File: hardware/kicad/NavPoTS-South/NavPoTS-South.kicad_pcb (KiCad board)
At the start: 4 copper layers, 58.9 x 58.9 mm, 119 parts, among them J1 Screw_Terminal_01x02, J10 Conn_01x03_Pin, J11 Conn_01x03_Pin, J12 Conn_01x03_Pin, J13 Conn_01x03_Pin, J14 Conn_01x03_Pin, J15 Conn_01x03_Pin, J16 Conn_01x03_Pin, J17 Screw_Terminal_01x02, J18 Conn_02x04_Top_Bottom, J19 Conn_02x04_Top_Bottom, J2 Screw_Terminal_01x02, J20 Screw_Terminal_01x02, J21 Screw_Terminal_01x02, J22 Conn_02x04_Top_Bottom, J23 62684-402100ALF, J24 Conn_02x04_Top_Bottom, J25 Screw_Terminal_01x02, J26 Screw_Terminal_01x02, J4 Screw_Terminal_01x02, J5 Screw_Terminal_01x02, J9 Conn_01x03_Pin, Q1 Q_NMOS_GSD, Q10 AO4576, Q11 AO4576, Q12 AO4576, Q13 AO4576, Q3 Q_NMOS_GSD, Q5 SI4143DY-T1-GE3, Q7 SI4143DY-T1-GE3, Q9 SI4143DY-T1-GE3, U1 SIC431A, U2 AP64501SP-13, U3 LTC4412xS6, U4 AP64501SP-13, U5 INA226

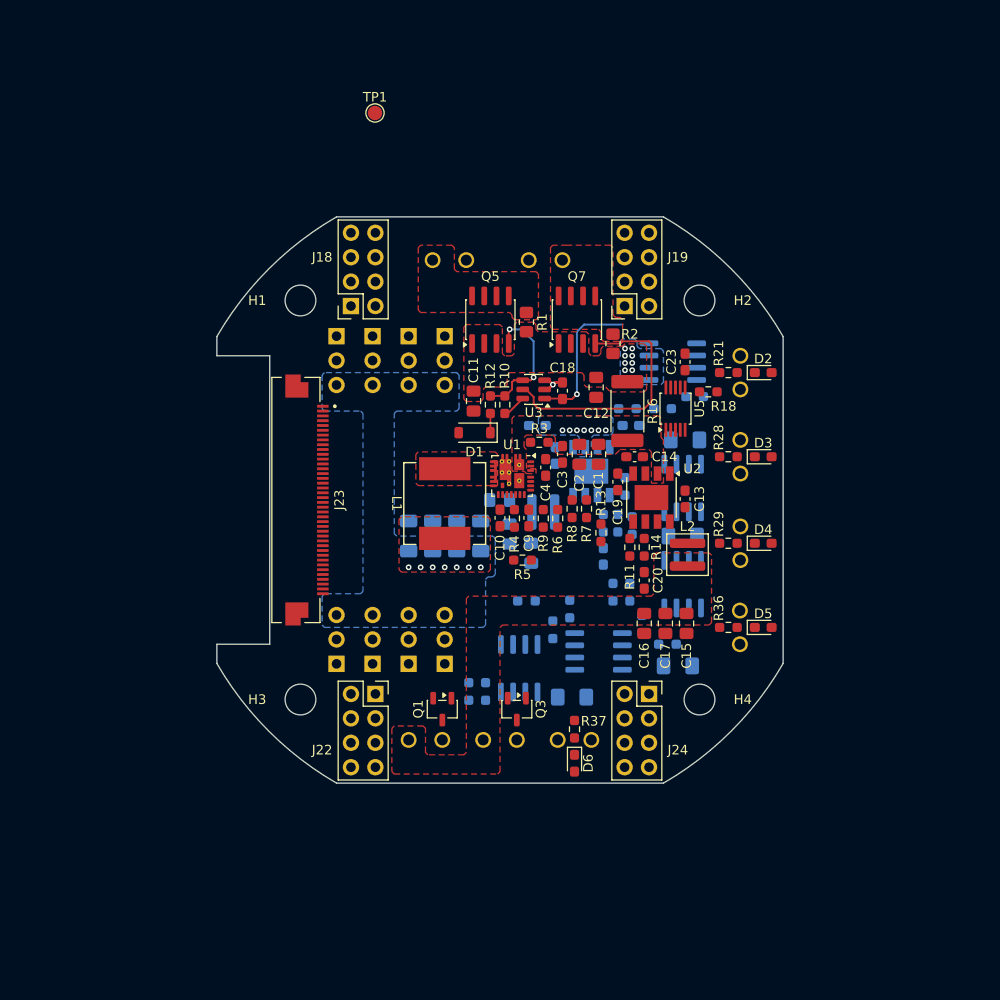
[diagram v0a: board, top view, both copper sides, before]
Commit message: first draft of south board routing
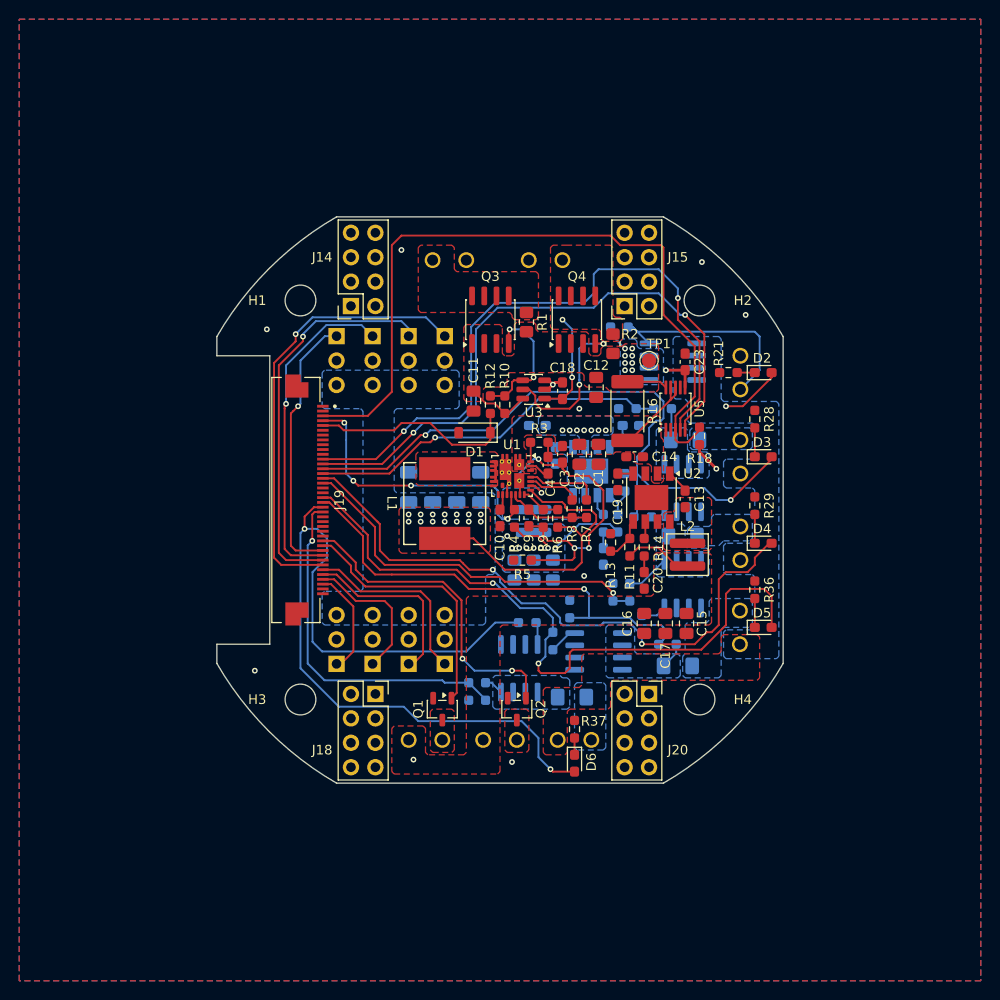
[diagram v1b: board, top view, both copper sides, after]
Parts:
- moved TP1 38.4 mm to (215.5, 85.5)
- moved R20 10.7 mm to (212.4, 82.0)
- moved C25 7.45 mm to (201.5, 107.3), turned to -90 degrees
- moved C5 5.06 mm to (198.0, 98.7)
- moved C6 5.06 mm to (195.5, 98.7)
- moved C7 5.06 mm to (193.0, 98.7)
- moved C8 5.06 mm to (190.5, 98.7)
- moved R28 4.78 mm to (226.5, 91.6), turned to 90 degrees
- moved R29 4.78 mm to (226.5, 100.6), turned to 90 degrees
- moved R36 4.78 mm to (226.5, 109.3), turned to 90 degrees
- moved R18 4.68 mm to (220.8, 93.3), turned to -90 degrees
- moved C26 4.51 mm to (203.5, 107.3)
- moved C24 2.85 mm to (205.5, 107.3)
- moved R33 2.25 mm to (202.8, 112.8)
- moved R24 1.42 mm to (214.8, 101.8), turned to 180 degrees
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- renumbered J14 to J10, J15 to J11, J16 to J12, J17 to J13, J18 to J14, J19 to J15, J20 to J16, J21 to J17, J22 to J18, J23 to J19, J24 to J20, J25 to J21, J26 to J22, J4 to J3, J5 to J4, J9 to J5, J10 to J6, J11 to J7, J12 to J8, J13 to J9, Q3 to Q2, Q5 to Q3, Q7 to Q4, Q9 to Q5, Q10 to Q6, Q11 to Q7, Q12 to Q8, Q13 to Q9
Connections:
- J19 pad 06: EXT_PWR0 -> unconnected-(J19-Pad06)
- J19 pad 07: EXT_PWR1 -> unconnected-(J19-Pad07)
- J19 pad 09: EXT_PWR2 -> unconnected-(J19-Pad09)
- J19 pad 28: EXT_PWR3 -> unconnected-(J19-Pad28)
- J19 pad 29: EXT_PWR4 -> EXT_PWR1
- J19 pad 30: EXT_PWR5 -> EXT_PWR0
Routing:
- net PYRO3_FIRE: track 0.00 -> 89.6 mm, vias 0 -> 2
- net V_ALERT: track 0.00 -> 78.3 mm
- net PYRO2_FIRE: track 0.00 -> 71.0 mm, vias 0 -> 2
- net PYRO0_FIRE: track 0.00 -> 69.9 mm, vias 0 -> 2
- net I2C1_SDA: track 0.00 -> 68.4 mm, vias 0 -> 2
- net PYRO1_FIRE: track 0.00 -> 64.5 mm, vias 0 -> 2
- net I2C1_SCL: track 0.00 -> 64.4 mm, vias 0 -> 2
- net PYRO2_CONTINUITY: track 0.00 -> 47.8 mm, vias 0 -> 1
- net PWM_3: track 0.00 -> 46.6 mm, vias 0 -> 1
- net PWM_2: track 0.00 -> 41.3 mm, vias 0 -> 1
- net PYRO1_CONTINUITY: track 0.00 -> 39.2 mm, vias 0 -> 1
- net PYRO0_CONTINUITY: track 0.00 -> 38.0 mm, vias 0 -> 1
- net PYRO3_CONTINUITY: track 0.00 -> 37.0 mm, vias 0 -> 1
- net PWM_1: track 0.00 -> 34.6 mm, vias 0 -> 1
- net GNDA: track 0.00 -> 33.5 mm, vias 0 -> 3
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- added copper zone on B.Cu, net +3V3
- added copper zone on In2.Cu, net +3V3
- added copper zone on B.Cu, net GND
- added copper zone on F.Cu, net GND
- added copper zone on In1.Cu, net GND
- added copper zone on B.Cu, net Net-(F1-Pad1)
- added copper zone on B.Cu, net Net-(F2-Pad1)
- added copper zone on B.Cu, net Net-(F3-Pad1)
- added copper zone on B.Cu, net Net-(F4-Pad1)
- added copper zone on F.Cu, net Net-(J1-Pin_2)
- added copper zone on B.Cu, net Net-(J16-Pin_2)
- added copper zone on B.Cu, net Net-(J17-Pin_2)
- added copper zone on B.Cu, net Net-(J21-Pin_2)
- added copper zone on B.Cu, net Net-(J22-Pin_2)
- added copper zone on F.Cu, net Net-(J4-Pin_2)
- added copper zone on F.Cu, net Net-(U2-SW)
- added copper zone on B.Cu, net Net-(U4-SW)
- added copper zone on B.Cu, net PYRO_HIGH_SIDE
- added copper zone on F.Cu, net PYRO_HIGH_SIDE
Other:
- board text removed: "${REFERENCE}"

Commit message: added gpio for future use on north and south boards
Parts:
- removed the J19 at (178.0, 100.0)
- added J18: 62684-402100ALF, custom:Amphenol_62684-402100ALF, F.Cu at (178.0, 100.0)
- renumbered J18 to J19

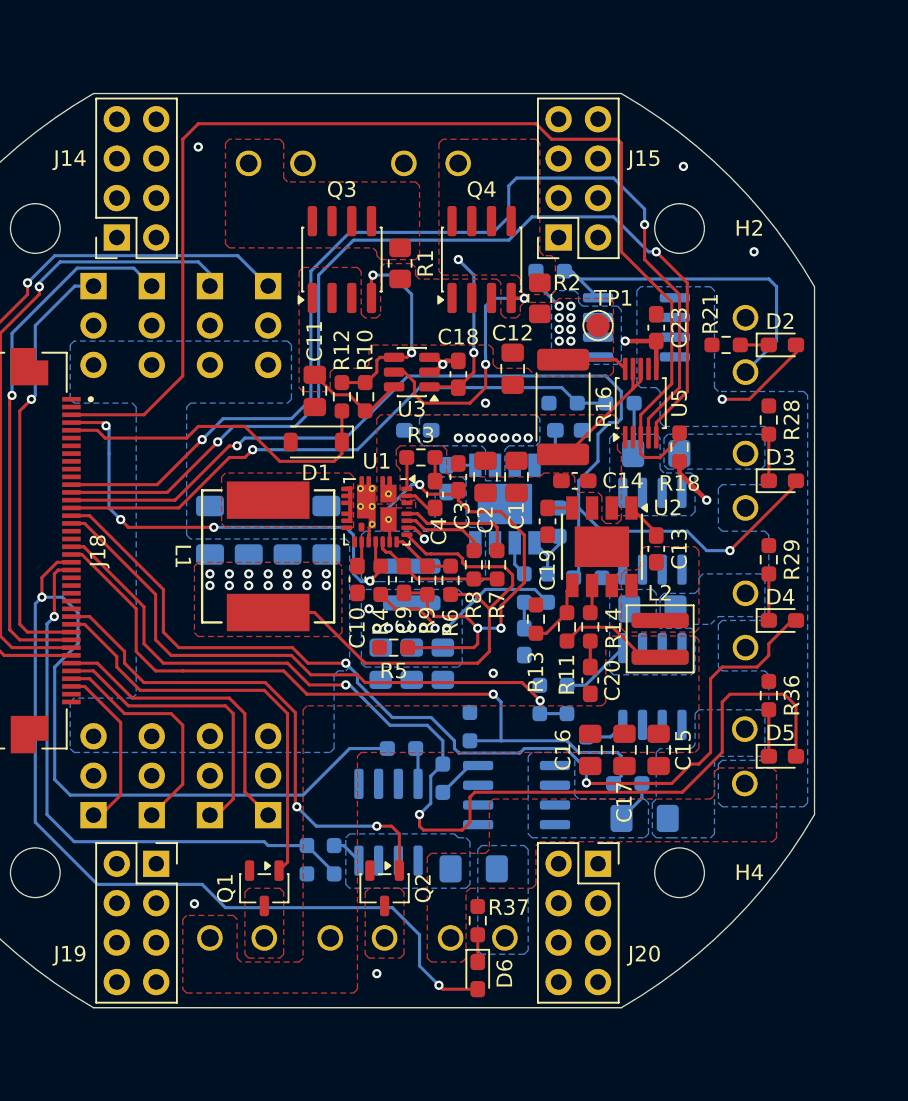
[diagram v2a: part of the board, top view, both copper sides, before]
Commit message: finished first draft of north pcb routing
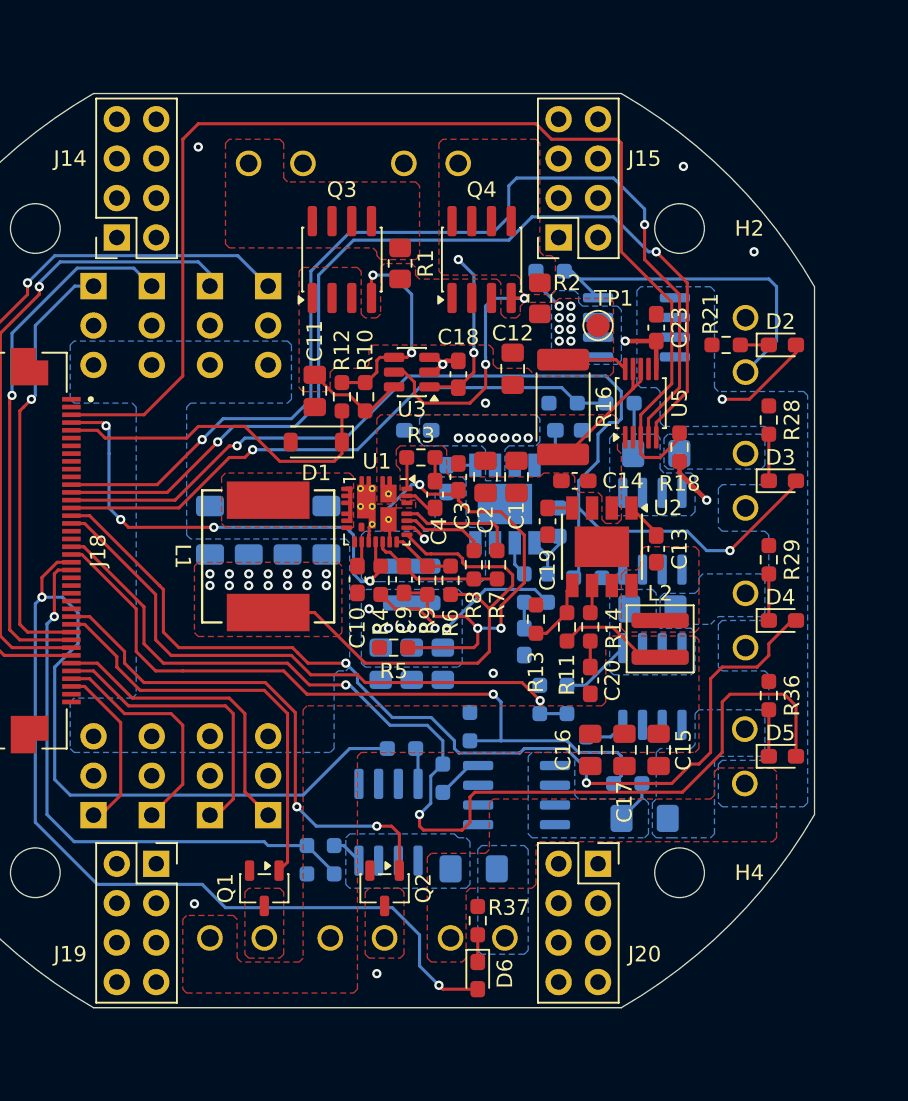
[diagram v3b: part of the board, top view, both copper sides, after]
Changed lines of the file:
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@@
 	(layers
 		(0 "F.Cu" signal)
-		(4 "In1.Cu" signal)
-		(6 "In2.Cu" signal)
+		(4 "In1.Cu" power)
+		(6 "In2.Cu" power)
 		(2 "B.Cu" signal)
 		(9 "F.Adhes" user "F.Adhesive")
@@
 	)
 	(gr_line
-		(start 216.999999 129.444863)
-		(end 183 129.444864)
+		(start 217 129.444863)
+		(end 183.000001 129.444864)
+		(stroke
+			(width 0.05)
+			(type solid)
+		)
+		(layer "Edge.Cuts")
+	)
+	(gr_line
+		(start 229.444864 83.000001)
+		(end 229.444864 116.999999)
 		(stroke
 			(width 0.05)
@@
 	)
 	(gr_arc
-		(start 216.999998 70.555136)
-		(mid 224.041629 75.958369)
-		(end 229.444862 83)
+		(start 217 70.555136)
+		(mid 224.041631 75.958369)
+		(end 229.444864 83)
 		(stroke
 			(width 0.05)
-			(type default)
+			(type solid)
 		)
 		(layer "Edge.Cuts")
@@
 	)
 	(gr_line
-		(start 229.444862 83)
-		(end 229.44485 117)
+		(start 216.999999 70.555136)
+		(end 183.000001 70.555136)
 		(stroke
 			(width 0.05)
-			(type default)
-		)
-		(layer "Edge.Cuts")
-	)
-	(gr_line
-		(start 216.999998 70.555136)
-		(end 183 70.555136)
-		(stroke
-			(width 0.05)
-			(type default)
+			(type solid)
 		)
 		(layer "Edge.Cuts")
 	)
 	(gr_arc
-		(start 229.444863 117)
-		(mid 224.04163 124.041631)
-		(end 216.999999 129.444864)
+		(start 229.444864 117)
+		(mid 224.041631 124.041631)
+		(end 217 129.444864)
 		(stroke
 			(width 0.05)
-			(type default)
+			(type solid)
 		)
 		(layer "Edge.Cuts")

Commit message: v1.0
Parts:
- added TP1: TestPoint, TestPoint:TestPoint_Pad_D1.5mm, B.Cu at (187.5, 99.5)
- added TP3: TestPoint, TestPoint:TestPoint_Pad_D1.5mm, F.Cu at (198.5, 111.8)
- added TP4: TestPoint, TestPoint:TestPoint_Pad_D1.5mm, B.Cu at (180.0, 96.2)
- renumbered J2 to J1, J1 to J2, TP1 to TP2
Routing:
- net +3V3: track 20.9 -> 23.9 mm, vias 10 -> 11
- net GND: vias 11 -> 15
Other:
- board text added: "v1.0 - 6/13/26 Luke Hooper"

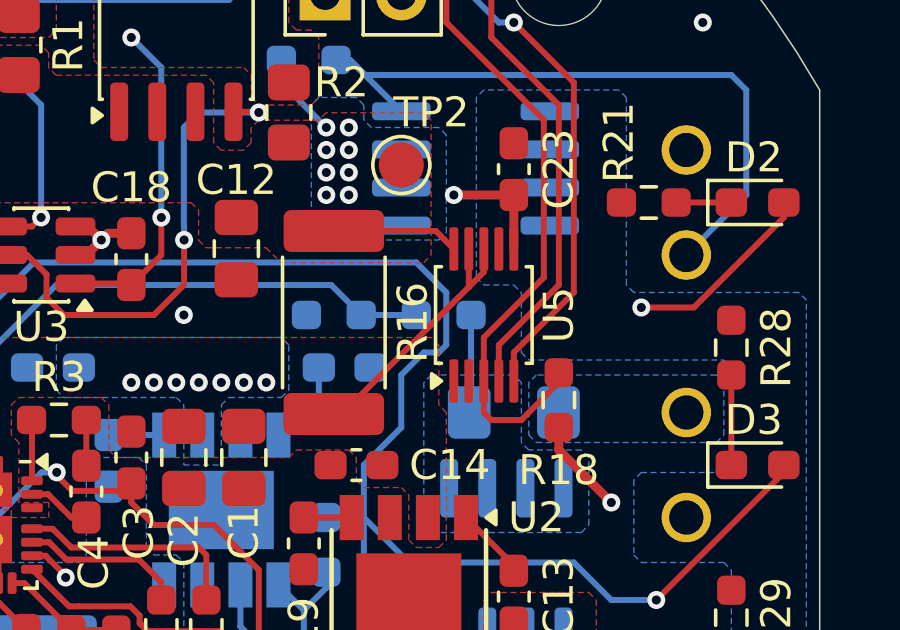
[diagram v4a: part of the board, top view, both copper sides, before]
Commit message: update to kicad, begin cad work for pcb holder bracket
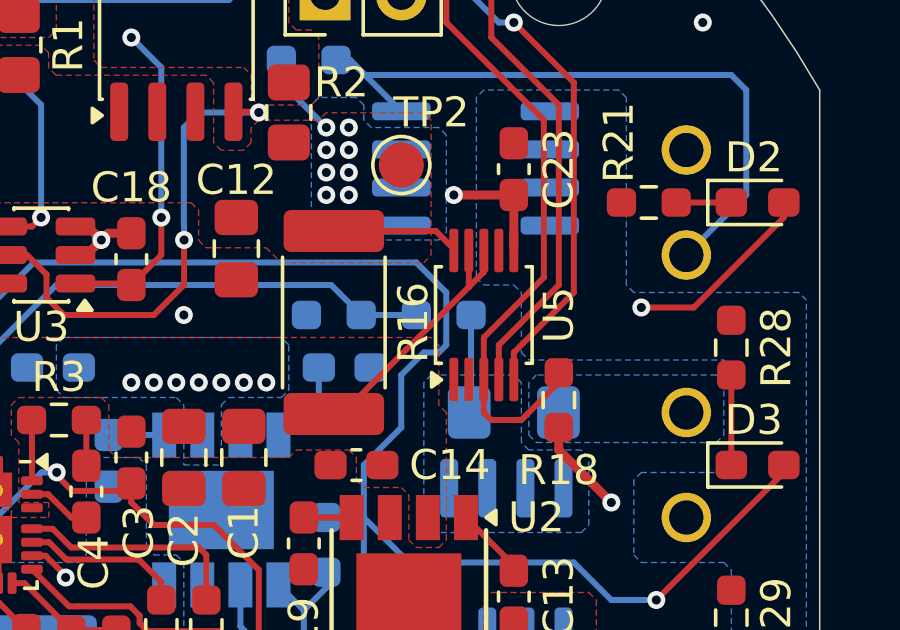
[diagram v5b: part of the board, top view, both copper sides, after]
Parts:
- U5: footprint Package_SO:VSSOP-10_3x3mm_P0.5mm -> Package_SO:TSSOP-10_3x3mm_P0.5mm
